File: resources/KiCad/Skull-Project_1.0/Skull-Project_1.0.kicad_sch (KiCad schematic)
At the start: 8 parts, among them SW1 SW_SPST, SW2 SW_SPST

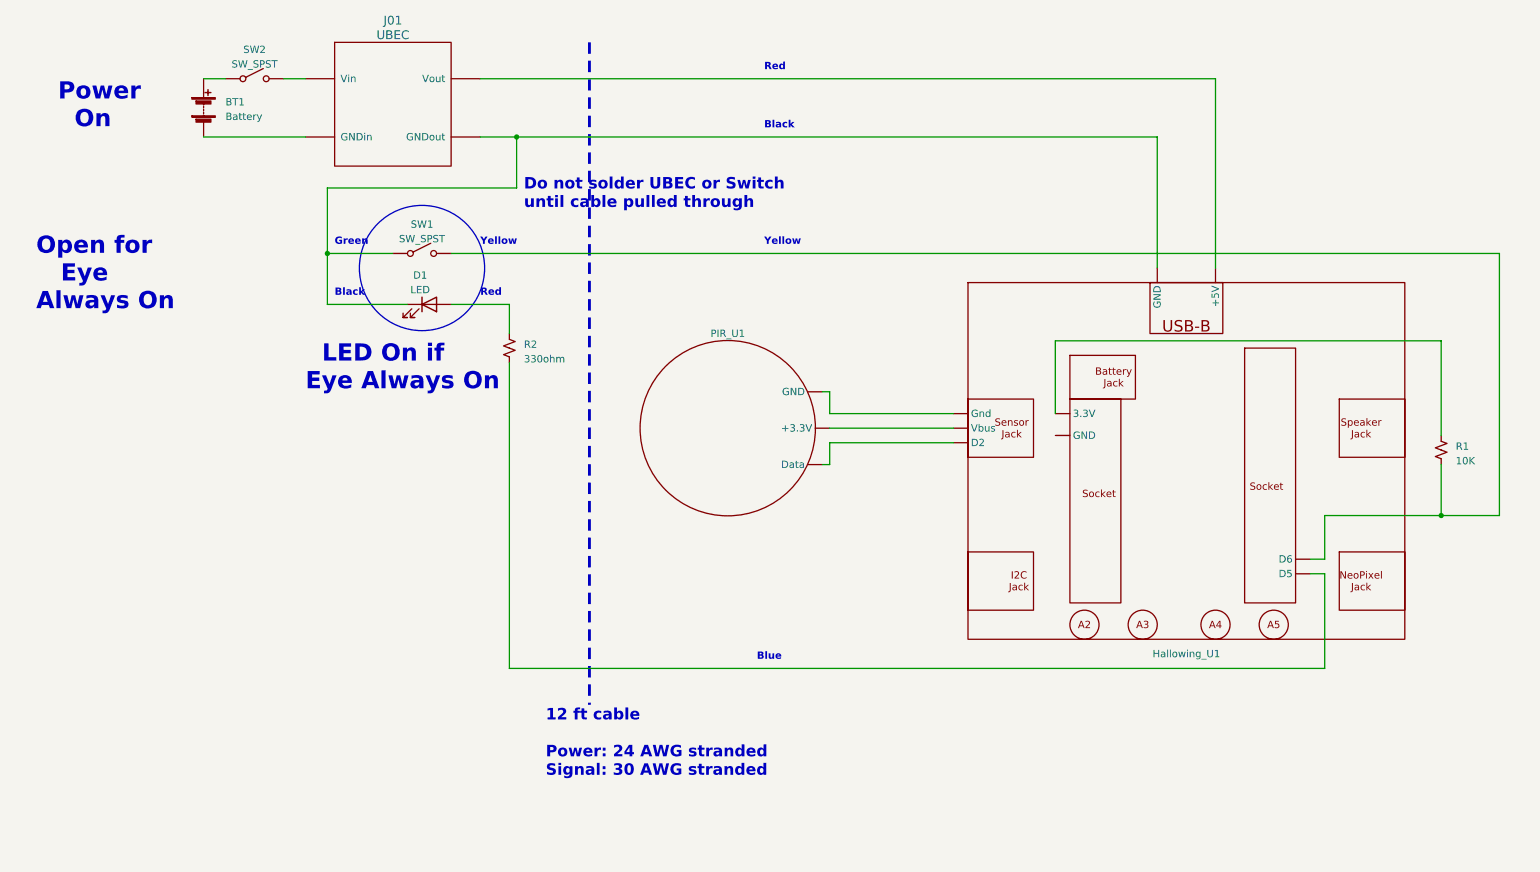
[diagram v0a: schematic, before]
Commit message: update schematic
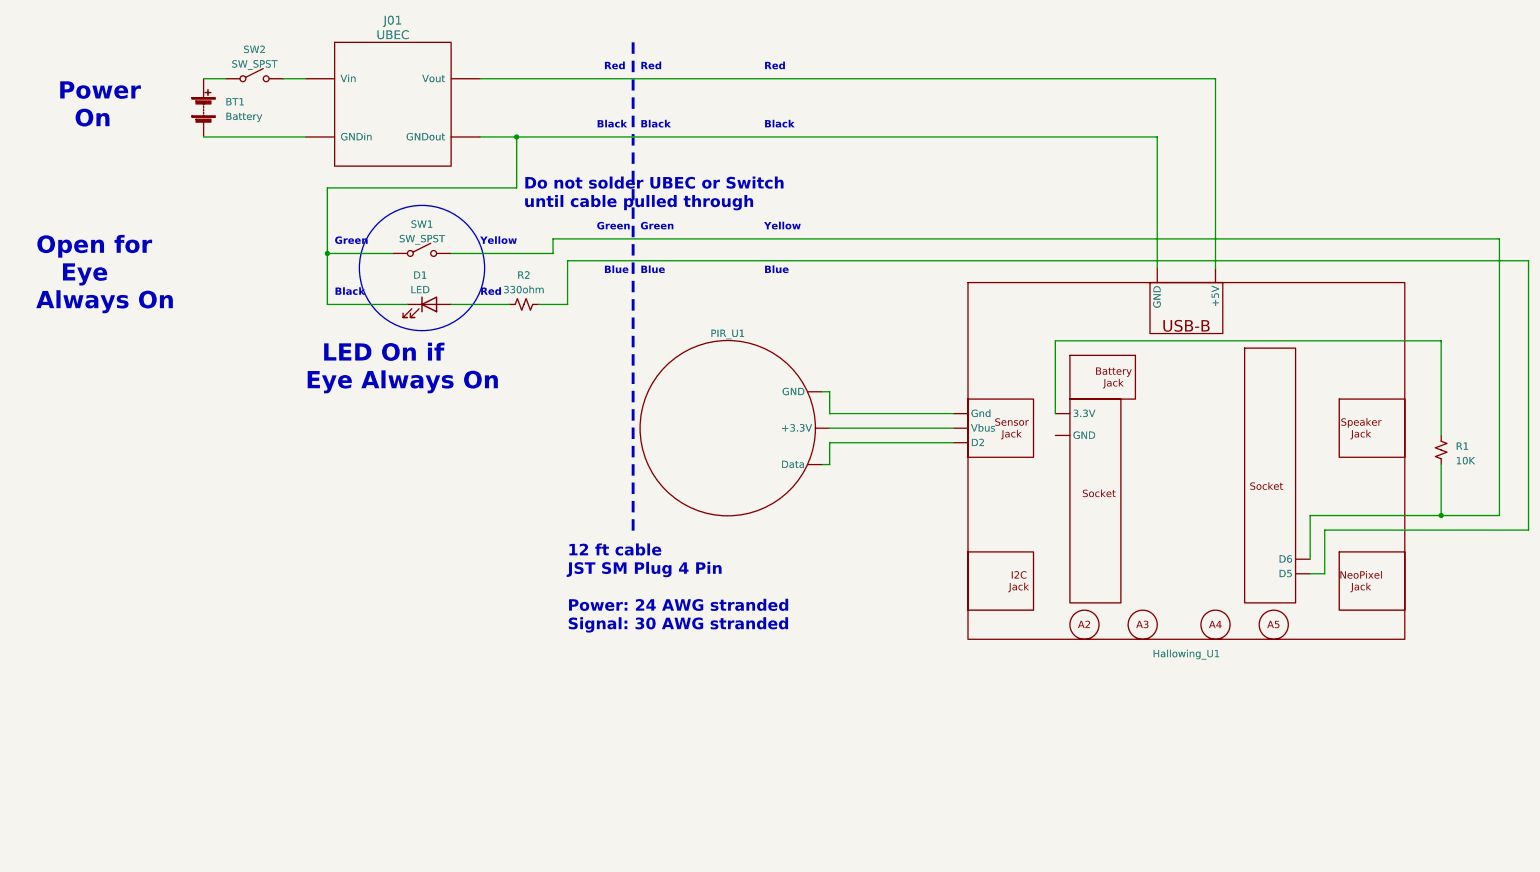
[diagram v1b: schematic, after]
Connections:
- net at Hallowing_U1. (Vbus): now also PIR_U1. (GND)
- net at SW2.~ (B): now also BT1.1 (+)
- new net: Hallowing_U1. (Vbus), R1.2, SW1.~ (B)
- new net: Hallowing_U1. (Vbus), PIR_U1. (GND) (x2)
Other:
- note added: "12 ft cable JST SM Plug 4 Pin Power: 24 AWG stranded Signal: 30 AWG stranded"
- note removed: "12 ft cable Power: 24 AWG stranded Signal: 30 AWG stranded"
- moved on the sheet: R2
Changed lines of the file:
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@@
-    (stroke (width 0) (type default))
-  )
-  (wire (pts (xy 92.71 58.42) (xy 275.59 58.42))
     (stroke (width 0) (type default))
   )
@@
     (stroke (width 0) (type default))
   )
+  (wire (pts (xy 245.11 114.3) (xy 245.11 106.68))
+    (stroke (width 0) (type default))
+  )
   (wire (pts (xy 97.79 38.1) (xy 104.14 38.1))
     (stroke (width 0) (type default))
   )
-  (wire (pts (xy 245.11 114.3) (xy 245.11 130.81))
-    (stroke (width 0) (type default))
-  )
   (wire (pts (xy 198.12 73.66) (xy 198.12 86.36))
     (stroke (width 0) (type default))
   )
+  (wire (pts (xy 280.67 106.68) (xy 280.67 59.69))
+    (stroke (width 0) (type default))
+  )
+  (wire (pts (xy 107.95 67.31) (xy 113.03 67.31))
+    (stroke (width 0) (type default))
+  )
+  (wire (pts (xy 245.11 106.68) (xy 280.67 106.68))
+    (stroke (width 0) (type default))
+  )
   (wire (pts (xy 158.75 91.44) (xy 180.34 91.44))
     (stroke (width 0) (type default))
   )
-  (polyline (pts (xy 116.84 21.59) (xy 116.84 137.16))
+  (polyline (pts (xy 124.46 21.59) (xy 124.46 107.95))
     (stroke (width 0.5) (type dash))
   )
@@
     (stroke (width 0) (type default))
   )
+  (wire (pts (xy 110.49 58.42) (xy 92.71 58.42))
+    (stroke (width 0) (type default))
+  )
   (wire (pts (xy 104.14 46.99) (xy 71.12 46.99))
     (stroke (width 0) (type default))
   )
-  (wire (pts (xy 102.87 72.39) (xy 102.87 67.31))
-    (stroke (width 0) (type default))
-  )
-  (wire (pts (xy 102.87 77.47) (xy 102.87 130.81))
+  (wire (pts (xy 242.57 104.14) (xy 242.57 111.76))
     (stroke (width 0) (type default))
   )
@@
     (stroke (width 0) (type default))
   )
-  (wire (pts (xy 265.43 104.14) (xy 245.11 104.14))
+  (wire (pts (xy 242.57 104.14) (xy 265.43 104.14))
     (stroke (width 0) (type default))
   )
@@
     (stroke (width 0) (type default))
   )
-  (wire (pts (xy 245.11 104.14) (xy 245.11 111.76))
-    (stroke (width 0) (type default))
-  )
   (wire (pts (xy 49.53 27.94) (xy 53.34 27.94))
     (stroke (width 0) (type default))
@@
     (stroke (width 0) (type default))
   )
-  (wire (pts (xy 242.57 111.76) (xy 245.11 111.76))
-    (stroke (width 0) (type default))
-  )
   (wire (pts (xy 104.14 38.1) (xy 215.9 38.1))
     (stroke (width 0) (type default))
@@
     (stroke (width 0) (type default))
   )
-  (wire (pts (xy 275.59 58.42) (xy 275.59 104.14))
+  (wire (pts (xy 275.59 55.88) (xy 275.59 104.14))
+    (stroke (width 0) (type default))
+  )
+  (wire (pts (xy 113.03 59.69) (xy 113.03 67.31))
     (stroke (width 0) (type default))
   )
@@
     (stroke (width 0) (type default))
   )
+  (wire (pts (xy 110.49 55.88) (xy 110.49 58.42))
+    (stroke (width 0) (type default))
+  )
   (wire (pts (xy 157.48 82.55) (xy 158.75 82.55))
     (stroke (width 0) (type default))
   )
-  (wire (pts (xy 245.11 130.81) (xy 102.87 130.81))
-    (stroke (width 0) (type default))
-  )
   (wire (pts (xy 63.5 27.94) (xy 67.31 27.94))
     (stroke (width 0) (type default))
   )
+  (wire (pts (xy 280.67 59.69) (xy 113.03 59.69))
+    (stroke (width 0) (type default))
+  )
   (wire (pts (xy 158.75 86.36) (xy 180.34 86.36))
     (stroke (width 0) (type default))
   )
+  (wire (pts (xy 275.59 55.88) (xy 110.49 55.88))
+    (stroke (width 0) (type default))
+  )
   (wire (pts (xy 49.53 38.1) (xy 67.31 38.1))
     (stroke (width 0) (type default))
@@
     (fill (type none))
   )
+  (text "Blue" (at 119.38 62.23 0)
+    (effects (font (size 1.27 1.27) bold) (justify left bottom))
+  )
   (text "Red" (at 97.79 66.04 0)
     (effects (font (size 1.27 1.27) bold) (justify left bottom))
   )
   (text "Black" (at 72.39 66.04 0)
-    (effects (font (size 1.27 1.27) bold) (justify left bottom))
-  )
-  (text "Blue" (at 146.05 129.54 0)
     (effects (font (size 1.27 1.27) bold) (justify left bottom))
   )
@@
     (effects (font (size 3 3) (thickness 0.6) bold) (justify left bottom))
   )
+  (text "Green" (at 125.73 54.61 0)
+    (effects (font (size 1.27 1.27) (thickness 0.254) bold) (justify left bottom))
+  )
   (text "Green" (at 72.39 57.15 0)
     (effects (font (size 1.27 1.27) (thickness 0.254) bold) (justify left bottom))
   )
+  (text "Blue" (at 147.32 62.23 0)
+    (effects (font (size 1.27 1.27) bold) (justify left bottom))
+  )
+  (text "Red" (at 125.73 26.67 0)
+    (effects (font (size 1.27 1.27) bold) (justify left bottom))
+  )
   (text "Yellow" (at 97.79 57.15 0)
     (effects (font (size 1.27 1.27) bold) (justify left bottom))
   )
-  (text "12 ft cable\n\nPower: 24 AWG stranded\nSignal: 30 AWG stranded"
-    (at 109.22 149.86 0)
+  (text "Blue" (at 125.73 62.23 0)
+    (effects (font (size 1.27 1.27) bold) (justify left bottom))
+  )
+  (text "Green" (at 118.11 54.61 0)
+    (effects (font (size 1.27 1.27) (thickness 0.254) bold) (justify left bottom))
+  )
+  (text "12 ft cable\nJST SM Plug 4 Pin\n\nPower: 24 AWG stranded\nSignal: 30 AWG stranded"
+    (at 113.03 124.46 0)
     (effects (font (size 2 2) (thickness 0.4) bold) (justify left bottom))
   )
@@
     (effects (font (size 3 3) (thickness 0.6) bold) (justify left bottom))
   )
-  (text "Yellow" (at 147.32 57.15 0)
+  (text "Yellow" (at 147.32 54.61 0)
+    (effects (font (size 1.27 1.27) bold) (justify left bottom))
+  )
+  (text "Black" (at 118.11 36.83 0)
     (effects (font (size 1.27 1.27) bold) (justify left bottom))
   )
@@
     (effects (font (size 3 3) (thickness 0.6) bold) (justify left bottom))
   )
+  (text "Black" (at 125.73 36.83 0)
+    (effects (font (size 1.27 1.27) bold) (justify left bottom))
+  )
   (text "Black" (at 147.32 36.83 0)
+    (effects (font (size 1.27 1.27) bold) (justify left bottom))
+  )
+  (text "Red" (at 119.38 26.67 0)
     (effects (font (size 1.27 1.27) bold) (justify left bottom))
   )
@@
     )
   )
-  (symbol (lib_id "Device:R_Small_US") (at 102.87 74.93 0) (unit 1)
+  (symbol (lib_id "Device:R_Small_US") (at 105.41 67.31 90) (unit 1)
     (in_bom yes) (on_board yes) (dnp no) (fields_autoplaced)
-    (property "Reference" "R2" (at 105.41 74.295 0)
-      (effects (font (size 1.27 1.27)) (justify left))
-    )
-    (property "Value" "330ohm" (at 105.41 76.835 0)
-      (effects (font (size 1.27 1.27)) (justify left))
-    )
-    (property "Footprint" "" (at 102.87 74.93 0)
-      (effects (font (size 1.27 1.27)) hide)
-    )
-    (property "Datasheet" "~" (at 102.87 74.93 0)
-      (effects (font (size 1.27 1.27)) hide)
-    )
+    (property "Reference" "R2" (at 105.41 62.23 90)
+      (effects (font (size 1.27 1.27)))
+    )
+    (property "Value" "330ohm" (at 105.41 64.77 90)
+      (effects (font (size 1.27 1.27)))
+    )
+    (property "Footprint" "" (at 105.41 67.31 0)
+      (effects (font (size 1.27 1.27)) hide)
+    )
+    (property "Datasheet" "~" (at 105.41 67.31 0)
+      (effects (font (size 1.27 1.27)) hide)
+    )

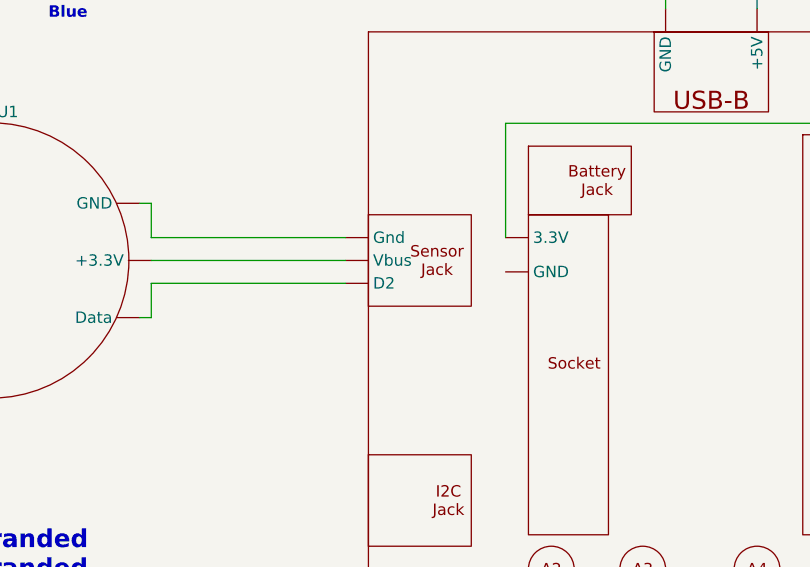
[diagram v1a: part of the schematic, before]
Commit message: update schematic
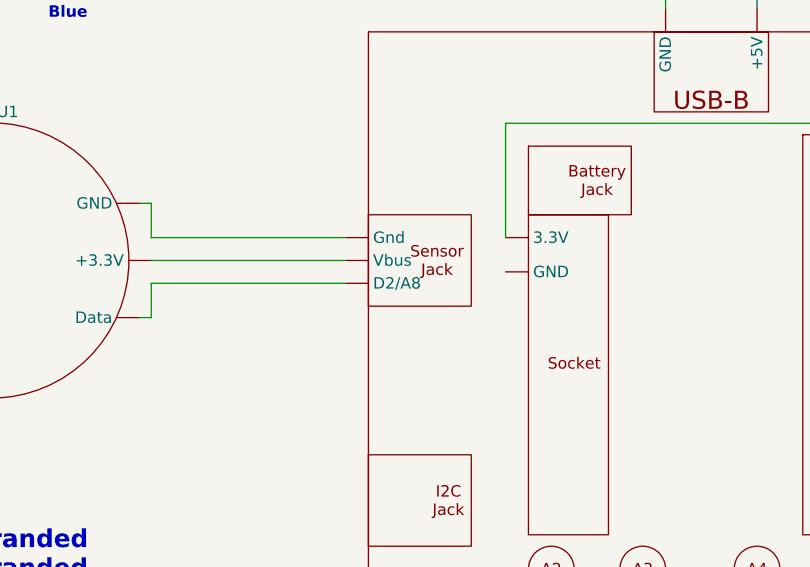
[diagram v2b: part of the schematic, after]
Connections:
- net at Hallowing_U1. (Vbus): now also PIR_U1. (GND)
- net at SW2.~ (B): now also BT1.1 (+)
- new net: Hallowing_U1. (Vbus), R1.2, SW1.~ (B)
- new net: Hallowing_U1. (Vbus), PIR_U1. (GND) (x2)
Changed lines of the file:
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@@
   (title_block
     (title "Skull-Project 1.0")
-    (date "2024-09-05")
+    (date "2024-09-07")
     (rev "1.0")
     (company "github.com/Mark-MDO47/Skull-Project")

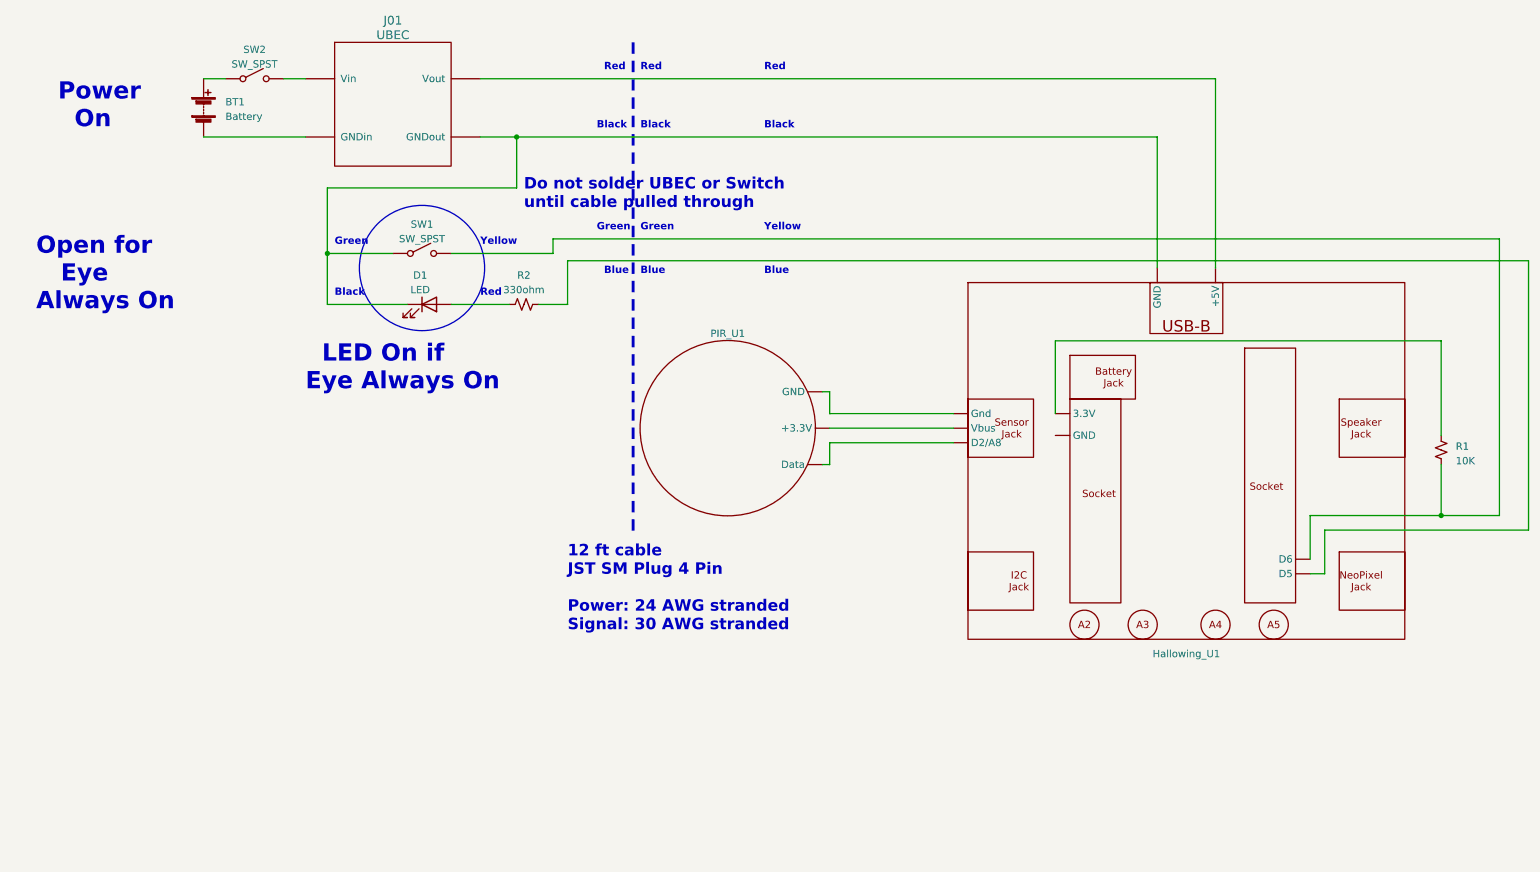
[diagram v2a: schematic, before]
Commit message: update schematic
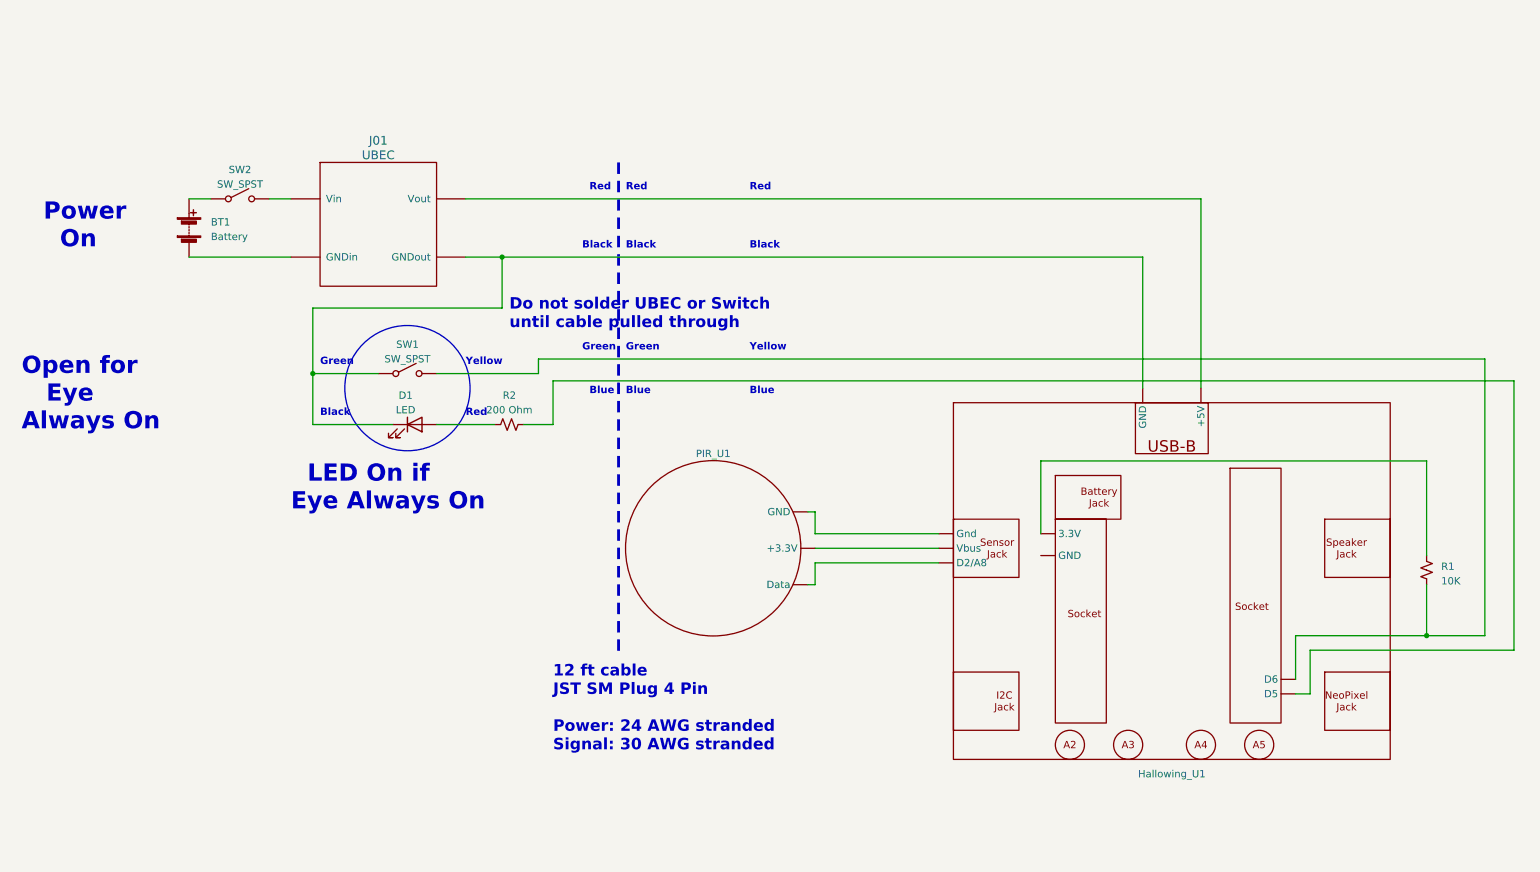
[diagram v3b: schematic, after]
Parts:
- R2: value 330ohm -> 200 Ohm
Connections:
- net at Hallowing_U1. (Vbus): now also PIR_U1. (GND)
- net at SW2.~ (B): now also BT1.1 (+)
- new net: Hallowing_U1. (Vbus), R1.2, SW1.~ (B)
- new net: Hallowing_U1. (Vbus), PIR_U1. (GND) (x2)
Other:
- moved on the sheet: BT1, D1, Hallowing_U1, PIR_U1, R1, R2, SW1, SW2
